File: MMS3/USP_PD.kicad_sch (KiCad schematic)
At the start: 4 parts, among them J801 USB_PD

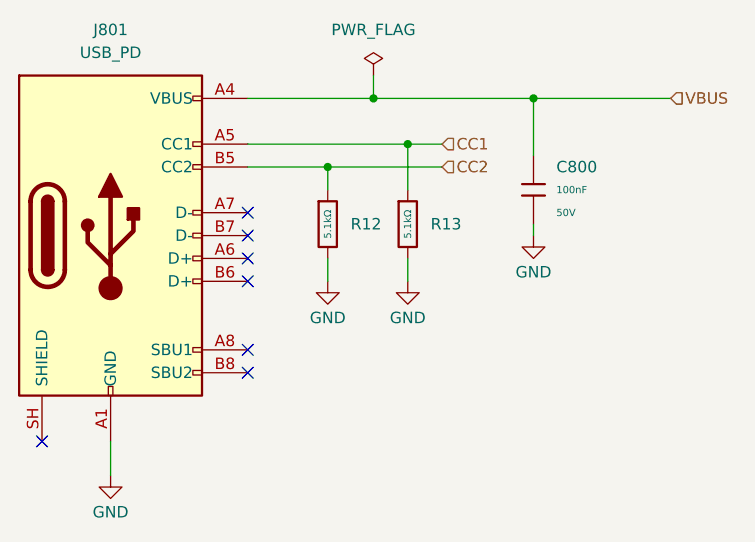
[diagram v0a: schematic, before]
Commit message: updated schematic, removed annotation
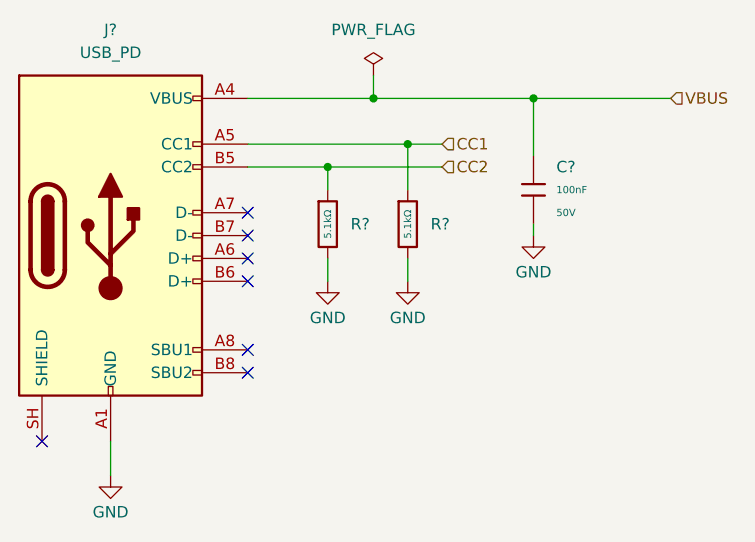
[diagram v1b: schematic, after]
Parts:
- renumbered C800 to C?, J801 to J?, R12 to R?, R13 to R?
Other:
- title: MMS3 -> MMS3 CH32L103 Version
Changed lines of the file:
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@@
 	(paper "A4")
 	(title_block
-		(title "MMS3")
+		(title "MMS3 CH32L103 Version")
+		(date "2026-05-18")
 		(rev "XA1")
 		(company "(c) Modular Mechanica")
-		(comment 1 "Artem Horiunov")
-		(comment 2 "DESIGNED IN POLAND")
+		(comment 1 "DESIGNED IN POLAND")
+		(comment 2 "Forked by: Wojciech Szafranski")
+		(comment 3 "Made by: Artem Horiunov")
 	)
 	(junction
@@
 		(in_pos_files yes)
 		(dnp no)
-		(property "Reference" "#PWR0810"
+		(property "Reference" "#PWR?"
 			(at 156.21 111.76 0)
 			(hide yes)
@@
 			(project "MMS3"
 				(path "/712cea22-140d-4c92-923f-f4998caf3ecd/e6704835-a0d6-4395-9f25-d1173d300c0c"
-					(reference "#PWR0810")
+					(reference "#PWR?")
 					(unit 1)
 				)
@@
 		(dnp no)
 		(fields_autoplaced yes)
-		(property "Reference" "C800"
+		(property "Reference" "C?"
 			(at 172.72 92.7099 0)
 			(show_name no)
@@
 			(project "MMS3"
 				(path "/712cea22-140d-4c92-923f-f4998caf3ecd/e6704835-a0d6-4395-9f25-d1173d300c0c"
-					(reference "C800")
+					(reference "C?")
 					(unit 1)
 				)
@@
 		(in_pos_files yes)
 		(dnp no)
-		(property "Reference" "#PWR0809"
+		(property "Reference" "#PWR?"
 			(at 147.32 111.76 0)
 			(hide yes)
@@
 			(project "MMS3"
 				(path "/712cea22-140d-4c92-923f-f4998caf3ecd/e6704835-a0d6-4395-9f25-d1173d300c0c"
-					(reference "#PWR0809")
+					(reference "#PWR?")
 					(unit 1)
 				)
@@
 		(dnp no)
 		(fields_autoplaced yes)
-		(property "Reference" "#FLG02"
+		(property "Reference" "#FLG?"
 			(at 152.4 80.645 0)
 			(hide yes)
@@
 			(project "MMS3"
 				(path "/712cea22-140d-4c92-923f-f4998caf3ecd/e6704835-a0d6-4395-9f25-d1173d300c0c"
-					(reference "#FLG02")
+					(reference "#FLG?")
 					(unit 1)
 				)
@@
 		(dnp no)
 		(fields_autoplaced yes)
-		(property "Reference" "R12"
+		(property "Reference" "R?"
 			(at 149.86 99.0599 0)
 			(show_name no)
@@
 			(project "MMS3"
 				(path "/712cea22-140d-4c92-923f-f4998caf3ecd/e6704835-a0d6-4395-9f25-d1173d300c0c"
-					(reference "R12")
+					(reference "R?")
 					(unit 1)
 				)
@@
 		(in_pos_files yes)
 		(dnp no)
-		(property "Reference" "#PWR0800"
+		(property "Reference" "#PWR?"
 			(at 170.18 106.68 0)
 			(hide yes)
@@
 			(project "MMS3"
 				(path "/712cea22-140d-4c92-923f-f4998caf3ecd/e6704835-a0d6-4395-9f25-d1173d300c0c"
-					(reference "#PWR0800")
+					(reference "#PWR?")
 					(unit 1)
 				)
@@
 		(dnp no)
 		(fields_autoplaced yes)
-		(property "Reference" "R13"
+		(property "Reference" "R?"
 			(at 158.75 99.0599 0)
 			(show_name no)
@@
 			(project "MMS3"
 				(path "/712cea22-140d-4c92-923f-f4998caf3ecd/e6704835-a0d6-4395-9f25-d1173d300c0c"
-					(reference "R13")
+					(reference "R?")
 					(unit 1)
 				)
@@
 		(dnp no)
 		(fields_autoplaced yes)
-		(property "Reference" "J801"
+		(property "Reference" "J?"
 			(at 123.19 77.47 0)
 			(show_name no)
@@
 			(project "MMS3"
 				(path "/712cea22-140d-4c92-923f-f4998caf3ecd/e6704835-a0d6-4395-9f25-d1173d300c0c"
-					(reference "J801")
+					(reference "J?")
 					(unit 1)
 				)
@@
 		(in_pos_files yes)
 		(dnp no)
-		(property "Reference" "#PWR0812"
+		(property "Reference" "#PWR?"
 			(at 123.19 133.35 0)
 			(hide yes)
@@
 			(project "MMS3"
 				(path "/712cea22-140d-4c92-923f-f4998caf3ecd/e6704835-a0d6-4395-9f25-d1173d300c0c"
-					(reference "#PWR0812")
+					(reference "#PWR?")
 					(unit 1)
 				)

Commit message: initial PCB update
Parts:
- gave numbers to parts that had none: 4
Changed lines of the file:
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@@
 		(in_pos_files yes)
 		(dnp no)
-		(property "Reference" "#PWR?"
+		(property "Reference" "#PWR0100"
 			(at 156.21 111.76 0)
 			(hide yes)
@@
 			(project "MMS3"
 				(path "/712cea22-140d-4c92-923f-f4998caf3ecd/e6704835-a0d6-4395-9f25-d1173d300c0c"
-					(reference "#PWR?")
+					(reference "#PWR0100")
 					(unit 1)
 				)
@@
 		(dnp no)
 		(fields_autoplaced yes)
-		(property "Reference" "C?"
+		(property "Reference" "C20"
 			(at 172.72 92.7099 0)
 			(show_name no)
@@
 			(project "MMS3"
 				(path "/712cea22-140d-4c92-923f-f4998caf3ecd/e6704835-a0d6-4395-9f25-d1173d300c0c"
-					(reference "C?")
+					(reference "C20")
 					(unit 1)
 				)
@@
 		(in_pos_files yes)
 		(dnp no)
-		(property "Reference" "#PWR?"
+		(property "Reference" "#PWR099"
 			(at 147.32 111.76 0)
 			(hide yes)
@@
 			(project "MMS3"
 				(path "/712cea22-140d-4c92-923f-f4998caf3ecd/e6704835-a0d6-4395-9f25-d1173d300c0c"
-					(reference "#PWR?")
+					(reference "#PWR099")
 					(unit 1)
 				)
@@
 		(dnp no)
 		(fields_autoplaced yes)
-		(property "Reference" "#FLG?"
+		(property "Reference" "#FLG03"
 			(at 152.4 80.645 0)
 			(hide yes)
@@
 			(project "MMS3"
 				(path "/712cea22-140d-4c92-923f-f4998caf3ecd/e6704835-a0d6-4395-9f25-d1173d300c0c"
-					(reference "#FLG?")
+					(reference "#FLG03")
 					(unit 1)
 				)
@@
 		(dnp no)
 		(fields_autoplaced yes)
-		(property "Reference" "R?"
+		(property "Reference" "R21"
 			(at 149.86 99.0599 0)
 			(show_name no)
@@
 			(project "MMS3"
 				(path "/712cea22-140d-4c92-923f-f4998caf3ecd/e6704835-a0d6-4395-9f25-d1173d300c0c"
-					(reference "R?")
+					(reference "R21")
 					(unit 1)
 				)
@@
 		(in_pos_files yes)
 		(dnp no)
-		(property "Reference" "#PWR?"
+		(property "Reference" "#PWR0101"
 			(at 170.18 106.68 0)
 			(hide yes)
@@
 			(project "MMS3"
 				(path "/712cea22-140d-4c92-923f-f4998caf3ecd/e6704835-a0d6-4395-9f25-d1173d300c0c"
-					(reference "#PWR?")
+					(reference "#PWR0101")
 					(unit 1)
 				)
@@
 		(dnp no)
 		(fields_autoplaced yes)
-		(property "Reference" "R?"
+		(property "Reference" "R22"
 			(at 158.75 99.0599 0)
 			(show_name no)
@@
 			(project "MMS3"
 				(path "/712cea22-140d-4c92-923f-f4998caf3ecd/e6704835-a0d6-4395-9f25-d1173d300c0c"
-					(reference "R?")
+					(reference "R22")
 					(unit 1)
 				)
@@
 		(dnp no)
 		(fields_autoplaced yes)
-		(property "Reference" "J?"
+		(property "Reference" "J5"
 			(at 123.19 77.47 0)
 			(show_name no)
@@
 			(project "MMS3"
 				(path "/712cea22-140d-4c92-923f-f4998caf3ecd/e6704835-a0d6-4395-9f25-d1173d300c0c"
-					(reference "J?")
+					(reference "J5")
 					(unit 1)
 				)
@@
 		(in_pos_files yes)
 		(dnp no)
-		(property "Reference" "#PWR?"
+		(property "Reference" "#PWR098"
 			(at 123.19 133.35 0)
 			(hide yes)
@@
 			(project "MMS3"
 				(path "/712cea22-140d-4c92-923f-f4998caf3ecd/e6704835-a0d6-4395-9f25-d1173d300c0c"
-					(reference "#PWR?")
+					(reference "#PWR098")
 					(unit 1)
 				)
